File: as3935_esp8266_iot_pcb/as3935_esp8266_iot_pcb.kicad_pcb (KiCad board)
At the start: 2 copper layers, 50 x 100 mm, 41 parts, among them K1 RELAY_2RT, K2 RELAY_2RT, P1 CONN_01X02, P2 CONN_01X02, P3 CONN_01X02, P4 CONN_01X08, P5 CONN_01X07, P6 CONN_01X03, P7 CONN_01X03, P8 CONN_01X06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

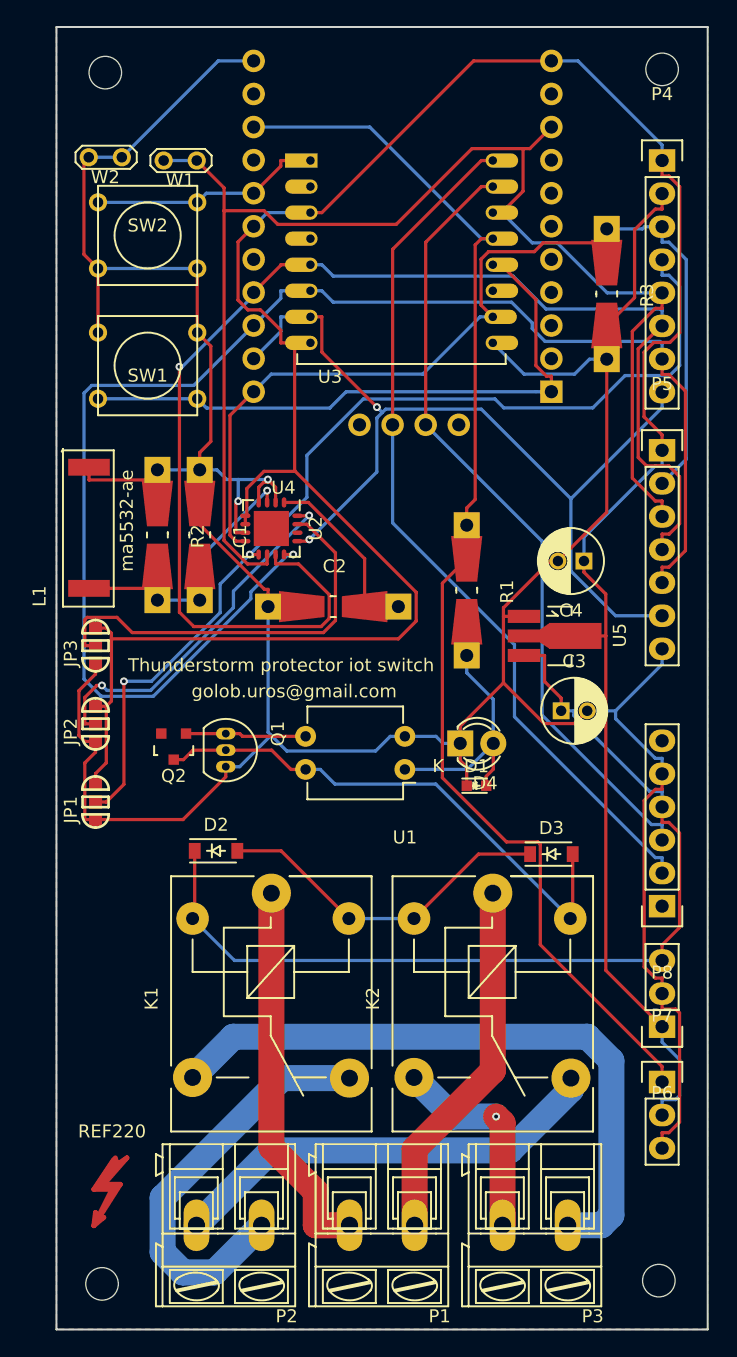
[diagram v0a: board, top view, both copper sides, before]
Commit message: new layout, added second transistor for relay,... digital side of pcb cal drive any relay board from ebay or something
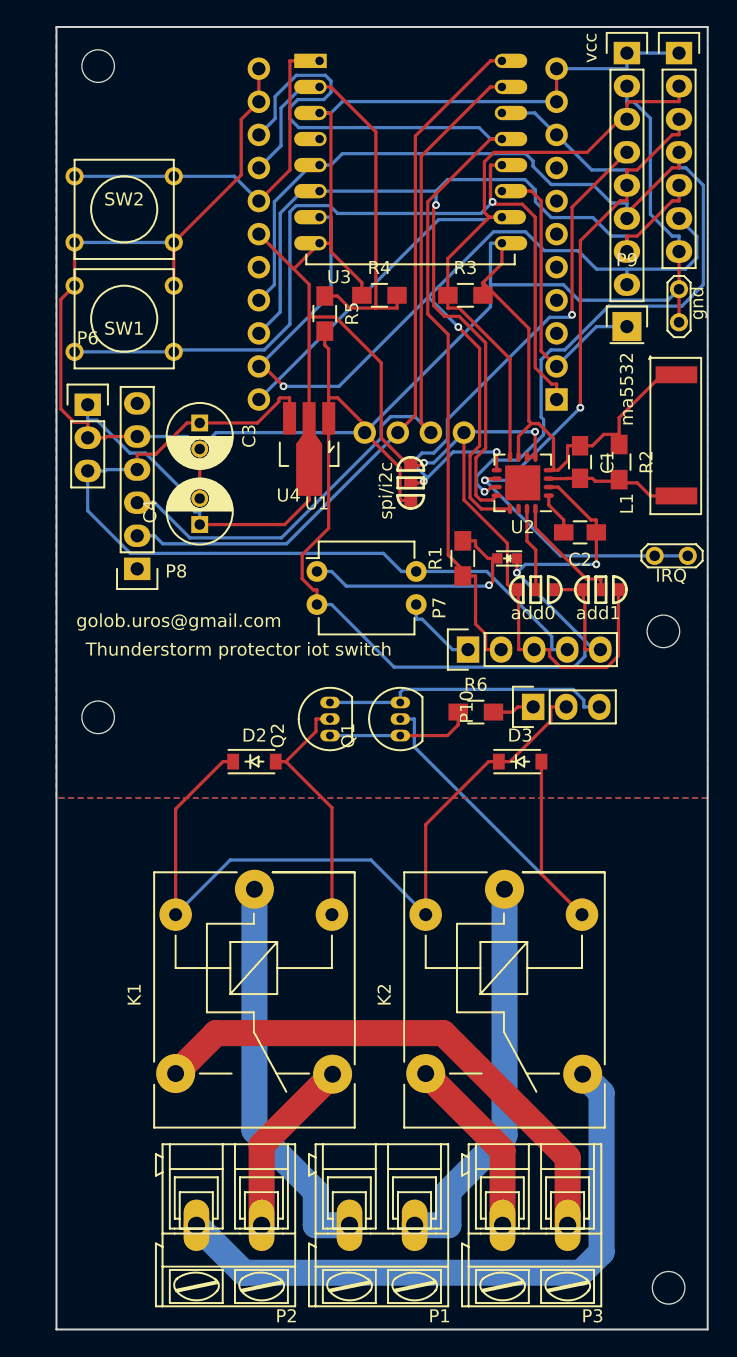
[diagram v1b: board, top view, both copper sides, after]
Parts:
- removed D4: LED, LEDs:LED-3MM
- removed REF220: Symbol_Highvoltage_Type1_CopperTop_Small, Symbols:Symbol_Highvoltage_Type1_CopperTop_Small
- added P10: CONN_01X03, Pin_Headers:Pin_Header_Straight_1x03, F.Cu at (56.6, 82.2)
- added P9: CONN_01X01, Pin_Headers:Pin_Header_Straight_1x01, F.Cu at (63.8, 53.0)
- added R4: R, Resistors_SMD:R_0805_HandSoldering, F.Cu at (44.8, 50.6)
- added R5: R, Resistors_SMD:R_0805_HandSoldering, F.Cu at (40.6, 52.0)
- added R6: R, Resistors_SMD:R_0805_HandSoldering, F.Cu at (52.2, 82.6)
- C1, C2: footprint Resistors_Universal:Resistor_SMD+THTuniversal_0805to1206_RM10_HandSoldering -> Capacitors_SMD:C_0805_HandSoldering
- P7: value CONN_01X03 -> CONN_01X05; footprint Pin_Headers:Pin_Header_Straight_1x03 -> Pin_Headers:Pin_Header_Straight_1x05
- Q2: value BC849 -> Q_NPN_BCE; footprint SOT-23 -> Housings_TO-92:TO-92_Inline_Narrow_Oval
- R1, R2, R3: footprint Resistors_Universal:Resistor_SMD+THTuniversal_0805to1206_RM10_HandSoldering -> Resistors_SMD:R_0805_HandSoldering
- moved P6 65.0 mm to (22.4, 59.0), turned to 0 degrees
- moved IRQ 48.4 mm to (67.2, 70.6)
- moved P8 47.9 mm to (26.2, 71.6)
- moved L1 45.7 mm to (67.6, 61.4)
- moved gnd 45.5 mm to (67.8, 51.4), turned to 90 degrees
- moved REF3 43.5 mm to (23.2, 83.0)
- moved REF2 43.2 mm to (66.6, 76.4)
- moved add1 40.1 mm to (61.8, 73.2), turned to 180 degrees
- moved P7 36.4 mm to (51.6, 77.8), turned to 90 degrees
- moved R2 35.9 mm to (63.2, 63.4)
- moved C3 35.5 mm to (31.0, 60.4), turned to 270 degrees
- moved spi/i2c 34.4 mm to (47.2, 65.0)
- moved add0 34.1 mm to (56.8, 73.2), turned to 0 degrees
- moved P5 30.5 mm to (67.8, 32.0)
- moved C1 29.7 mm to (60.2, 63.4)
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- renumbered W1 to IRQ, JP3 to add0, JP2 to add1, W2 to gnd, JP1 to spi/i2c, P4 to vcc
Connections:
- D3 pad 1: Net-(D2-Pad2) -> +5V
- K2 pad 8: Net-(D2-Pad2) -> +5V
- P7 pad 1: /to_sw -> /to_switch
- P7 pad 2: +3V3 -> /to_sw
- P7 pad 3: GND -> +3V3
- P8 pad 1: Net-(P8-Pad1) -> (no net)
- P8 pad 6: Net-(P8-Pad6) -> (no net)
- Q2 pad 2: GND -> Net-(D2-Pad2)
- Q2 pad 3: Net-(D3-Pad2) -> GND
- U1 pad 3: Net-(Q1-Pad1) -> /to_switch
- U1 pad 4: Net-(D3-Pad2) -> +5V
- U2 pad 14: Net-(U2-Pad14) -> (no net)
- U3 pad 11: Net-(U3-Pad11) -> Net-(P9-Pad1)
- U3 pad 2: Net-(U3-Pad2) -> /adc
- U3 pad 4: Net-(U3-Pad4) -> (no net)
- U4 pad 10: Net-(U4-Pad10) -> +3V3
- U4 pad 13: Net-(U4-Pad13) -> GND
- U4 pad 15: Net-(U4-Pad15) -> /adc
- U4 pad 18: Net-(U4-Pad18) -> (no net)
- U4 pad 2: Net-(U4-Pad2) -> Net-(P9-Pad1)
- U4 pad 23: Net-(U4-Pad23) -> GND
- U4 pad 26: Net-(U4-Pad26) -> +3V3
- U4 pad 3: Net-(U4-Pad3) -> (no net)
- U4 pad 4: Net-(U4-Pad4) -> (no net)
- U4 pad 5: Net-(U4-Pad5) -> (no net)
- U4 pad 6: Net-(U4-Pad6) -> (no net)
- U4 pad 7: Net-(U4-Pad7) -> (no net)
- U4 pad 8: Net-(U4-Pad8) -> (no net)
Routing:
- net +3V3: track 214.5 -> 158.4 mm, vias 0 -> 2
- net +5V: track 73.9 -> 123.9 mm
- net /irq: track 107.5 -> 67.5 mm, vias 0 -> 2
- net /miso: track 114.5 -> 76.5 mm
- net /adc: track 0.00 -> 35.1 mm
- net /si: track 76.8 -> 42.5 mm, vias 2 -> 3
- net /add0: track 32.0 -> 6.48 mm
- net Net-(P9-Pad1): track 0.00 -> 23.2 mm
- net /to_sw: track 97.2 -> 76.8 mm
- net /add1: track 27.8 -> 8.93 mm, vias 2 -> 0
- net Net-(K1-Pad1): track 32.1 -> 13.9 mm
- net /flash: track 47.8 -> 64.9 mm, vias 0 -> 1
- net /clk: track 103.0 -> 87.6 mm
- net Net-(C1-Pad2): track 25.1 -> 10.5 mm, vias 1 -> 0
- net Net-(K2-Pad1): track 33.9 -> 47.5 mm
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
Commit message: small redesign
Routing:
- net /to_sw: track 76.8 -> 113.4 mm, vias 0 -> 1
- net /irq: track 67.5 -> 92.1 mm, vias 2 -> 1
- net +3V3: track 158.4 -> 173.8 mm, vias 2 -> 1
- net /clk: track 87.6 -> 76.5 mm, vias 1 -> 2
- net +5V: track 123.9 -> 134.7 mm
- net Net-(D3-Pad2): track 34.5 -> 26.9 mm, vias 0 -> 1
- net /tx: track 56.2 -> 61.7 mm
- net /flash: track 64.9 -> 60.4 mm
- net /si: track 42.5 -> 38.1 mm
- net GND: track 277.7 -> 281.6 mm
- net /miso: track 76.5 -> 72.7 mm, vias 1 -> 2
- net Net-(D1-Pad2): track 19.3 -> 15.6 mm, vias 1 -> 0
- net /rx: track 58.5 -> 55.0 mm
- net /mosi: track 80.9 -> 78.3 mm, vias 2 -> 1
- net Net-(P9-Pad1): track 23.2 -> 21.7 mm, vias 0 -> 1
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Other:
- net class ac: clearance 0.6 -> 0.65
